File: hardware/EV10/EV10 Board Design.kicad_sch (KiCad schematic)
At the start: 107 parts, among them J11 Conn_01x06_Female, J12 Conn_01x04_Female, J13 Conn_01x04_Female, J2 Conn_01x02_Female, J3 Conn_01x02_Socket, J4 Conn_01x08_Male, J5 Conn_01x02_Socket, J6 Conn_01x04_Female, J7 Conn_01x04_Female, J8 Conn_01x06_Female, J9 USB_C_Receptacle, SW4 SW_Push, SW5 SW_Push, U1 STM32F405RGTx, U11 ESP32-S3-WROOM-1-N8R2, U13 BM14B(0.8)-24DS-0.4V(53), U2 MCP73832-2-OT, U3 CH340C, U4 USBLC6-2P6, U5 STM32F030C8Tx, U6 WM8960CGEFL/RV, U7 TPS63060, Y1 Crystal_GND24

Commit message: EV10 Design with new screen connector and pwr mgmt
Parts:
- removed J12, J6: Conn_01x04_Female, 1x4 pin download:1x4pin 1mm connector, symbol Connector:Conn_01x04_Female
- removed J3: Conn_01x02_Socket, Connector_JST:JST_PH_S2B-PH-SM4-TB_1x02-1MP_P2.00mm_Horizontal, symbol Connector:Conn_01x02_Socket
- removed J4: Conn_01x08_Male, Connector_PinHeader_2.54mm:PinHeader_1x08_P2.54mm_Vertical, symbol Connector:Conn_01x08_Male
- removed R28, R29: 10k, Resistor_SMD:R_0402_1005Metric, symbol Device:R
- removed U2: MCP73832-2-OT, Package_TO_SOT_SMD:SOT-23-5, symbol Battery_Management:MCP73832-2-OT
- added C2: 10u, Capacitor_SMD:C_0402_1005Metric, symbol Device:C
- added J1: Conn_01x02_Socket, Connector_JST:JST_PH_S2B-PH-SM4-TB_1x02-1MP_P2.00mm_Horizontal, symbol Connector:Conn_01x02_Socket
- added J10: Conn_01x08_Socket, Connector_JST:JST_SHL_SM08B-SHLS-TF_1x08-1MP_P1.00mm_Horizontal, symbol Connector:Conn_01x08_Socket
- added R22: 10k, Resistor_SMD:R_0402_1005Metric, symbol Device:R
- added U2: BQ21040DBVR, BQ21040DBVR:SOT95P280X145-6N, symbol BQ21040DBVR:BQ21040DBVR
- C1: value 4.7u -> 10u; footprint Capacitor_SMD:C_0805_2012Metric -> Capacitor_SMD:C_0402_1005Metric
- R26: value 1k -> 680
- R27: value 1k -> 1k5
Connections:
- net BATTERY_MON: no longer C1.1
- net DISP_BL: now also J10.1 (Pin_1)
- net DISP_CS: now also J10.4 (Pin_4)
- net DISP_DC: now also J10.3 (Pin_3)
- net DISP_RSTR: now also J10.2 (Pin_2)
- net DISP_SPI_MOSI: now also J10.6 (Pin_6)
- net DISP_SPI_SCK: now also J10.5 (Pin_5)
- net GND: now also R26.2, C2.2, J1.1 (Pin_1), J10.7 (Pin_7), R22.2, U2.5 (GND); no longer R26.1
- net VBUS: now also C1.1, U2.6 (VIN); no longer D1.2 (A)
- net VIN: now also J10.8 (Pin_8)
- net at R27.1: now also D2.2 (A), C2.1, J1.2 (Pin_2), U2.2 (OUT); no longer D1.1 (K)
- net at R27.2: now also D1.2 (A)
- net UI_RX1_NET renamed UI_RX2_NET
- net UI_SWDCLK: no longer names the net of U1.49 (PA14)
- net UI_SWDIO: no longer names the net of U1.46 (PA13)
- net UI_TX1_NET renamed UI_TX2_NET
- new net: R22.1, U2.1 (TS)
- new net: R26.1, U2.4 (ISET)
- new net: D1.1 (K), U2.3 (~{CHG})
- no-connect marks 75 -> 77
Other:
- note added: "Display - 1MM B"
- note added: "EV10 layer build up: top: High Speed second: GND third: 3.3V bottom: Low Speed"
- note removed: "BATT CONN"
- note removed: "Display - 2MM T"
- note removed: "EV9 layer build up: top: High Speed second: GND third: 3.3V bottom: Low Speed"
- note removed: "PROGRAM - 2MM L"
- moved on the sheet: 120R1, C10, C33, C37, C38, C39, C40, C41, C42, C43, C44, C45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

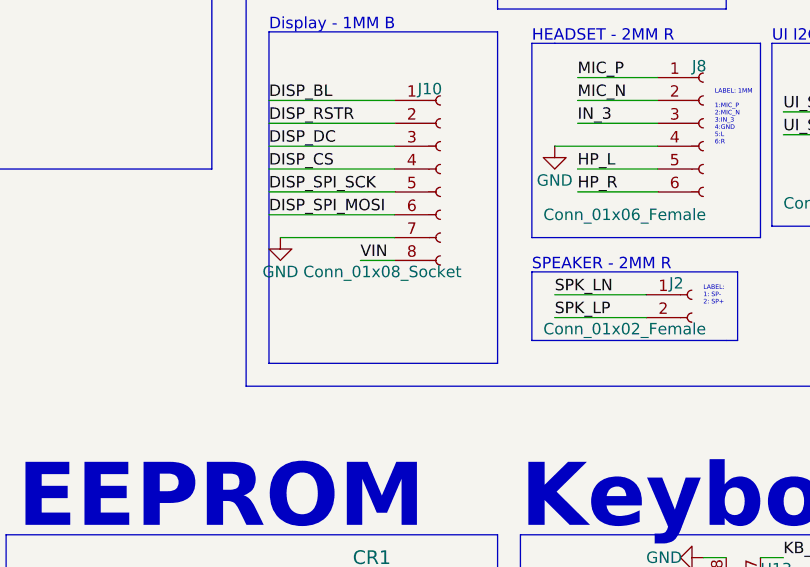
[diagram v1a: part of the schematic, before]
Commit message: EV10 bord design with V2 pwr mgmt and screen conn
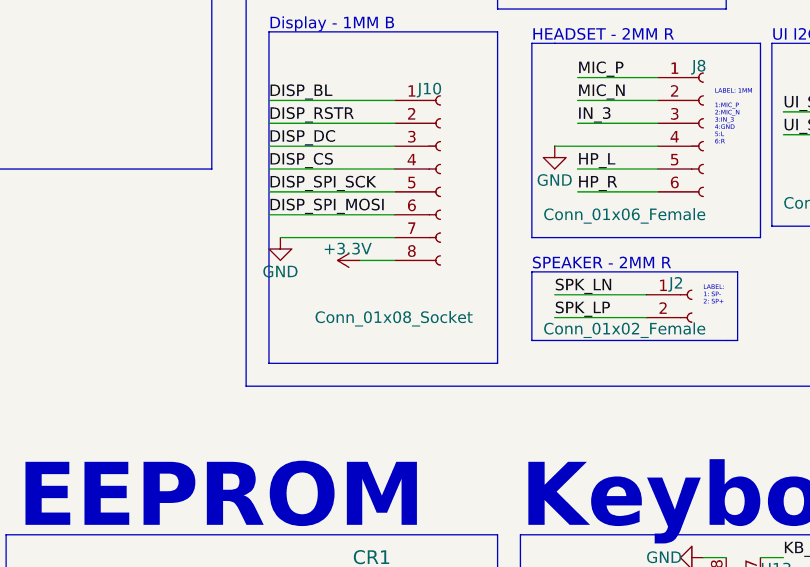
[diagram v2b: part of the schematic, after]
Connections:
- net VIN is gone; now on net +3.3V: J10.8 (Pin_8)
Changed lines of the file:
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@@
     (effects (font (size 1.27 1.27)) (justify right bottom))
   )
-  (label "VIN" (at 321.31 264.16 0) (fields_autoplaced)
-    (effects (font (size 1.27 1.27)) (justify left bottom))
-  )
   (label "LEDB_B" (at 129.54 109.22 0) (fields_autoplaced)
     (effects (font (size 1.27 1.27)) (justify left bottom))
@@
     )
   )
+  (symbol (lib_id "power:+3.3V") (at 321.31 264.16 90) (unit 1)
+    (in_bom yes) (on_board yes) (dnp no)
+    (property "Reference" "#PWR02" (at 325.12 264.16 0)
+      (effects (font (size 1.27 1.27)) hide)
+    )
+    (property "Value" "+3.3V" (at 322.58 262.89 90)
+      (effects (font (size 1.27 1.27)) (justify left))
+    )
+    (property "Footprint" "" (at 321.31 264.16 0)
+      (effects (font (size 1.27 1.27)) hide)
+    )
+    (property "Datasheet" "" (at 321.31 264.16 0)
+      (effects (font (size 1.27 1.27)) hide)
+    )
+    (pin "1")
+    (instances
+      (project "EV10 Board Design"
+        (path "/bd865368-262b-4f76-b7a6-1673c2cb0f8c"
+          (reference "#PWR02") (unit 1)
+        )
+      )
+    )
+  )
   (symbol (lib_id "Connector:USB_C_Receptacle") (at 66.04 237.49 180) (unit 1)
     (in_bom yes) (on_board yes) (dnp no)
@@
       (effects (font (size 1.27 1.27)) (justify left))
     )
-    (property "Value" "Conn_01x08_Socket" (at 314.96 265.43 0)
+    (property "Value" "Conn_01x08_Socket" (at 316.23 270.51 0)
       (effects (font (size 1.27 1.27)) (justify left))
     )

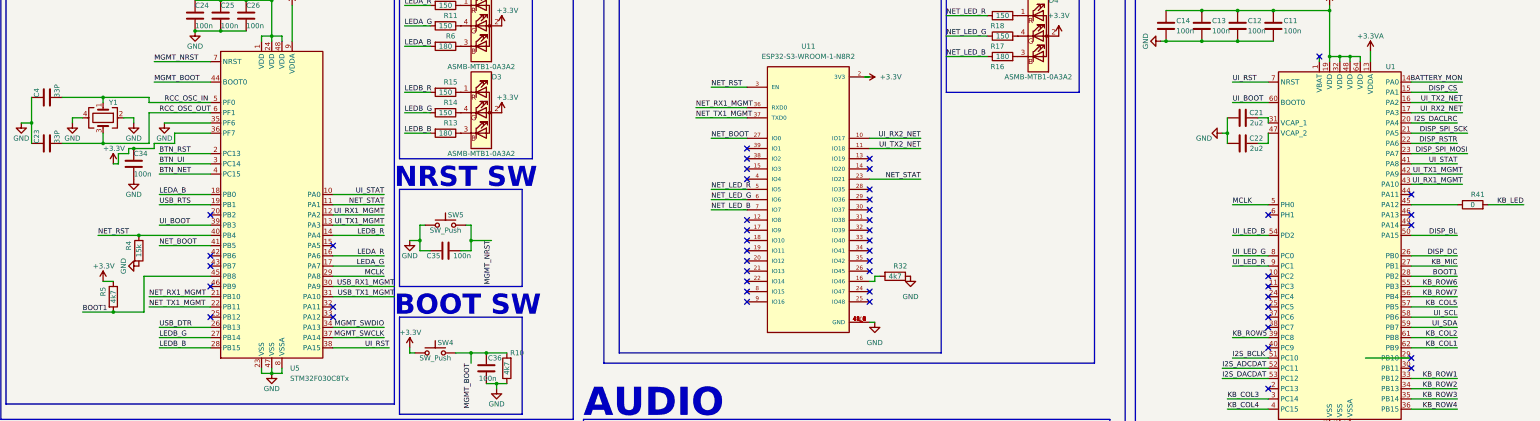
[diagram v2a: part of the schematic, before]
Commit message: Matched EV10 schematic labels with ioc
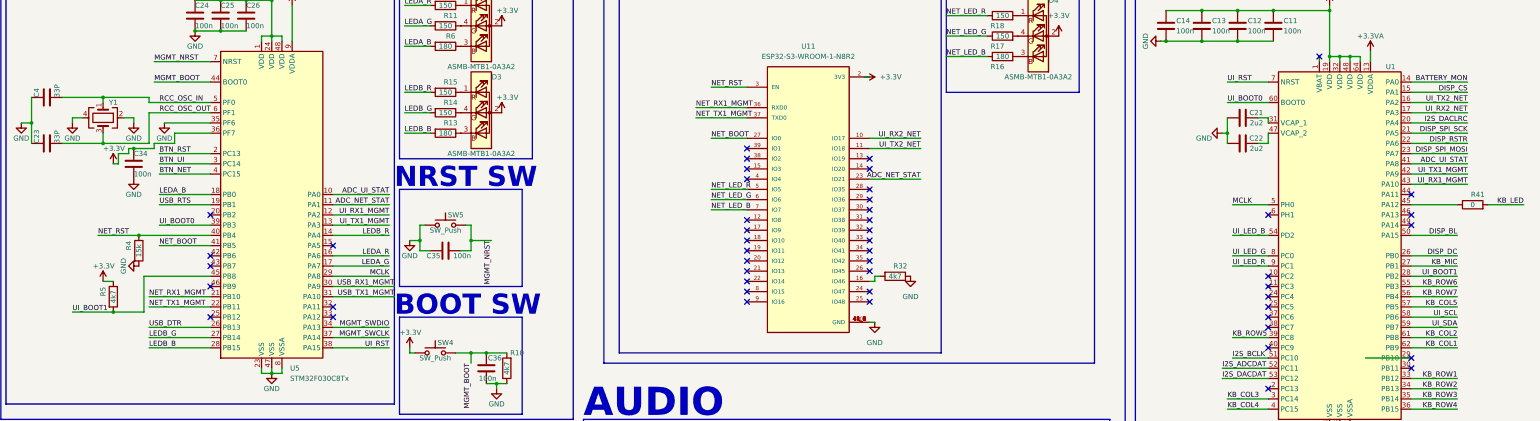
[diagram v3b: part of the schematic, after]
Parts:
- U6: symbol Audio Interface:WM8960CGEFL/RV -> Audio Interface:WM8960CGEFL/RV
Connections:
- net BOOT1 renamed UI_BOOT1
- net NET_STAT renamed ADC_NET_STAT
- net UI_BOOT renamed UI_BOOT0
- net UI_STAT renamed ADC_UI_STAT

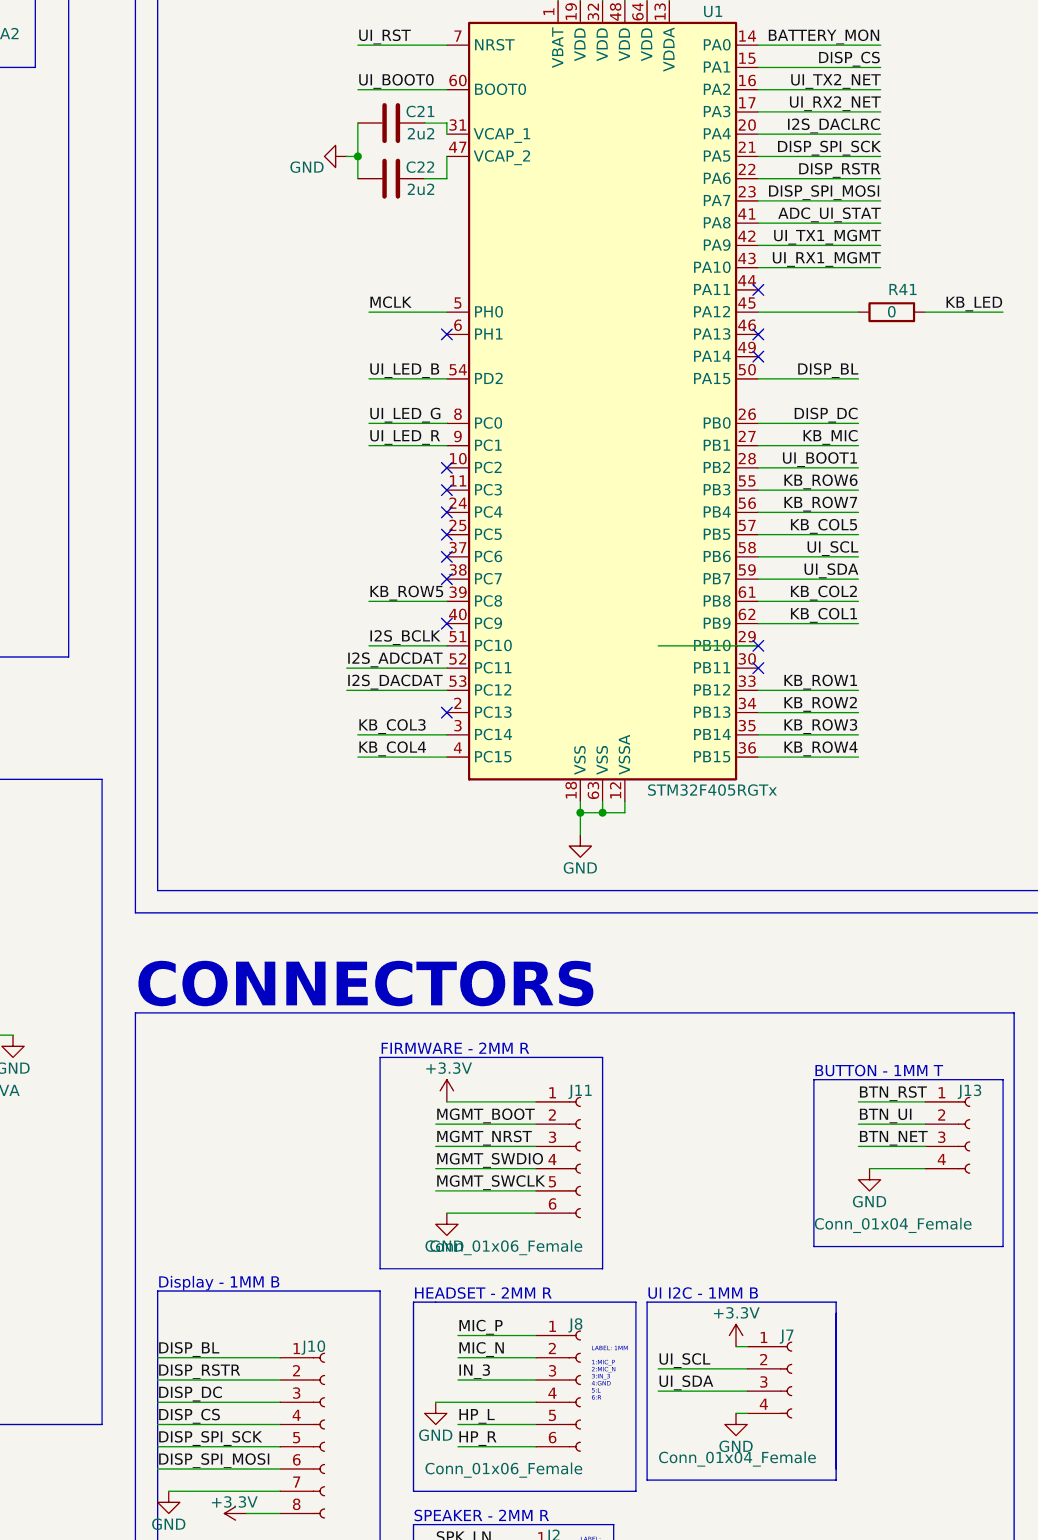
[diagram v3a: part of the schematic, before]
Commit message: Got all clocks correct, and audio incoming and outgoing
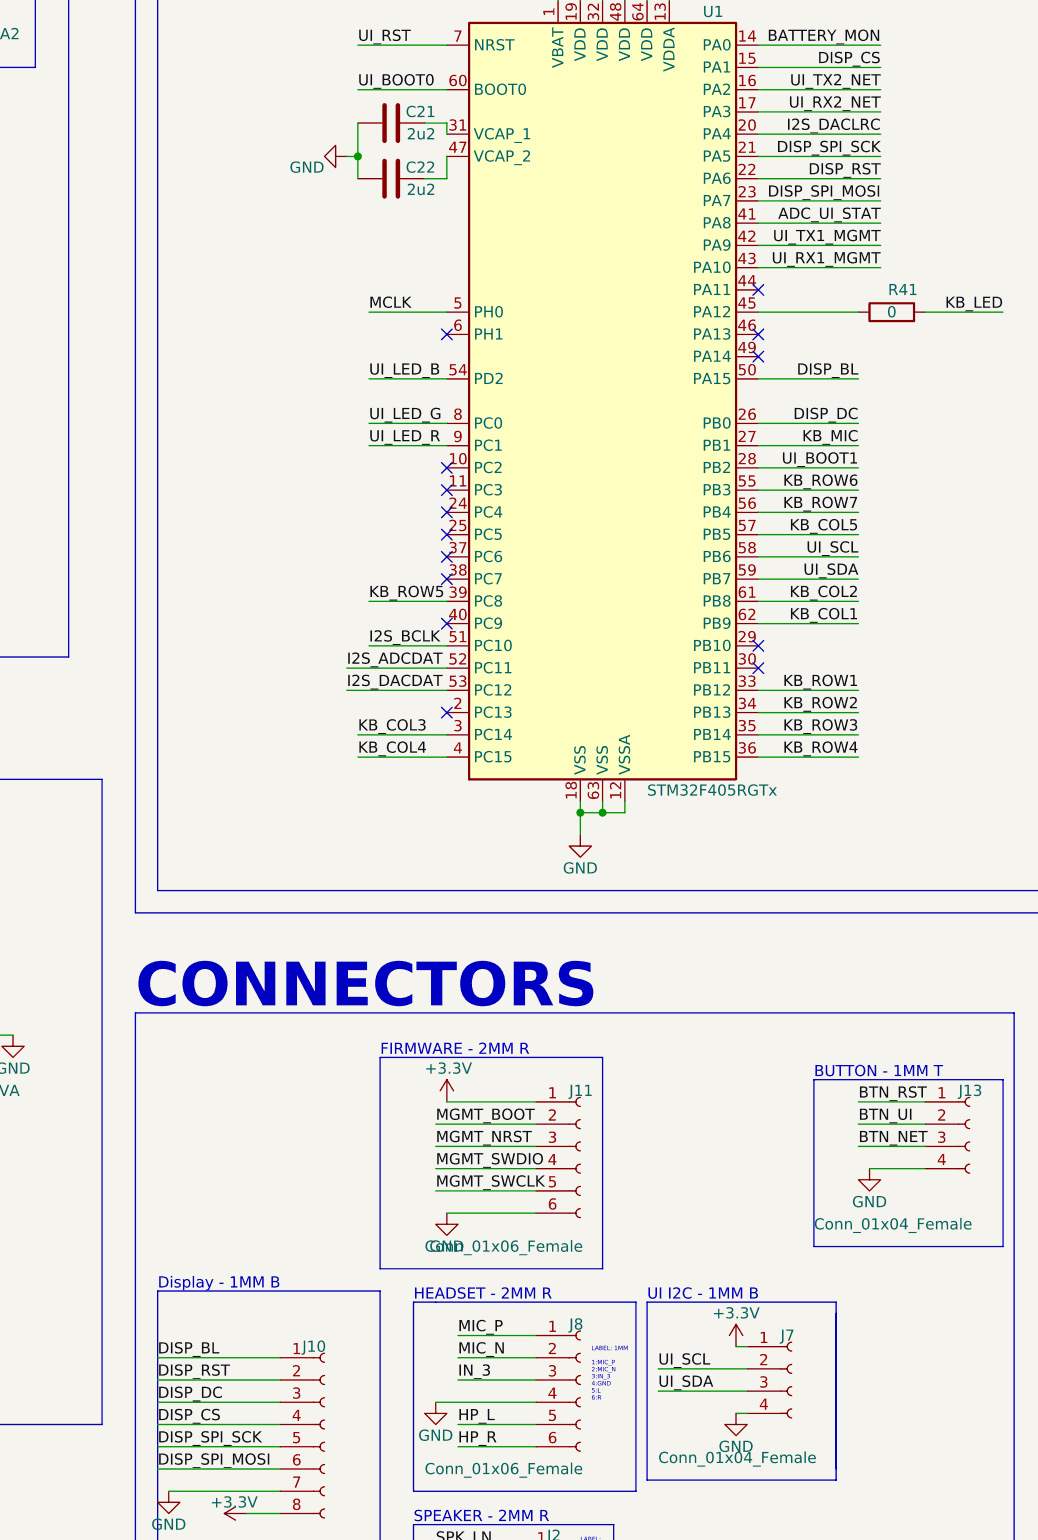
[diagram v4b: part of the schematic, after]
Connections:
- net DISP_RSTR renamed DISP_RST
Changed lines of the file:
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@@
-    (stroke (width 0) (type default))
-  )
-  (wire (pts (xy 379.73 165.1) (xy 368.3 165.1))
     (stroke (width 0) (type default))
   )
@@
     (effects (font (size 1.27 1.27)) (justify right bottom))
   )
-  (label "DISP_RSTR" (at 311.15 248.92 0) (fields_autoplaced)
+  (label "DISP_RST" (at 311.15 248.92 0) (fields_autoplaced)
     (effects (font (size 1.27 1.27)) (justify left bottom))
   )
@@
     (effects (font (size 1.27 1.27)) (justify right bottom))
   )
-  (label "DISP_RSTR" (at 393.7 111.76 180) (fields_autoplaced)
-    (effects (font (size 1.27 1.27)) (justify right bottom))
-  )
+  (label "DISP_RST" (at 393.7 111.76 180) (fields_autoplaced)
+    (effects (font (size 1.27 1.27)) (justify right bottom))
+  )
